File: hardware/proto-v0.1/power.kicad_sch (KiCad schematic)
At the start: 34 parts, among them J1 5V_EXT, U1 TPS2065C, U2 LP5907-3.3

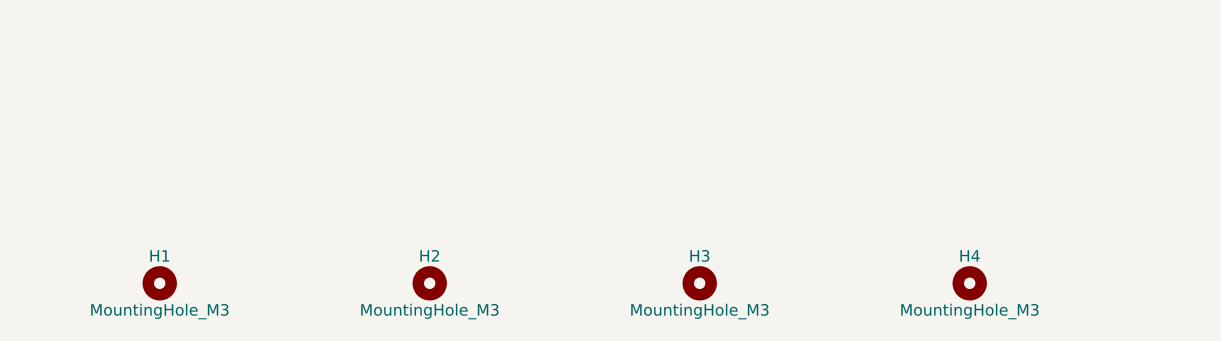
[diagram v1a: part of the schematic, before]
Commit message: Proto-PCB v0.1: fit Fischer AKG 105.26 case (100x80 mm)
Board 100x100 -> 100x80 mm, R1.5 mm corners, no mounting holes (slides into
case grooves), unmasked GND copper strips along both long edges, horizontal
BNC/SMA connectors for the 15.2 mm height budget, router/test-point fixes.
Docs updated to v0.18.

Co-Authored-By: Claude Sonnet 5.5 <noreply@anthropic.com>
Claude-Session: https://claude.ai/code/session_01BBEBh5Nhxyv6s49uSZkpLo
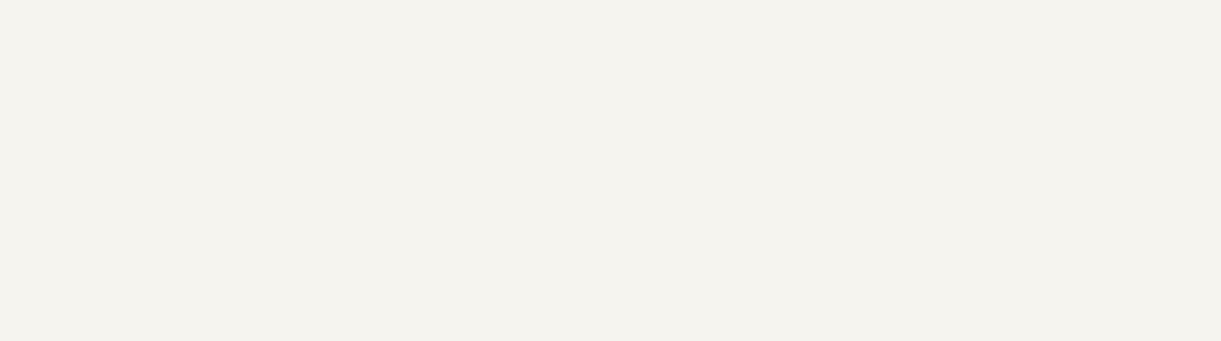
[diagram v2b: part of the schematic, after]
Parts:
- removed H1, H2, H3, H4: MountingHole_M3, MountingHole:MountingHole_3.2mm_M3, symbol Mechanical:MountingHole
